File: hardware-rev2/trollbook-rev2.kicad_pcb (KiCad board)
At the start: 2 copper layers, 160 x 120 mm, 1 part, among them U1 MC68040FC33V

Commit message: added fpga
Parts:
- added U2: EPF10K50VRC240, mod:RQFP-240, F.Cu at (173.0, 101.5)
- moved U1 23.9 mm to (125.6, 101.1)

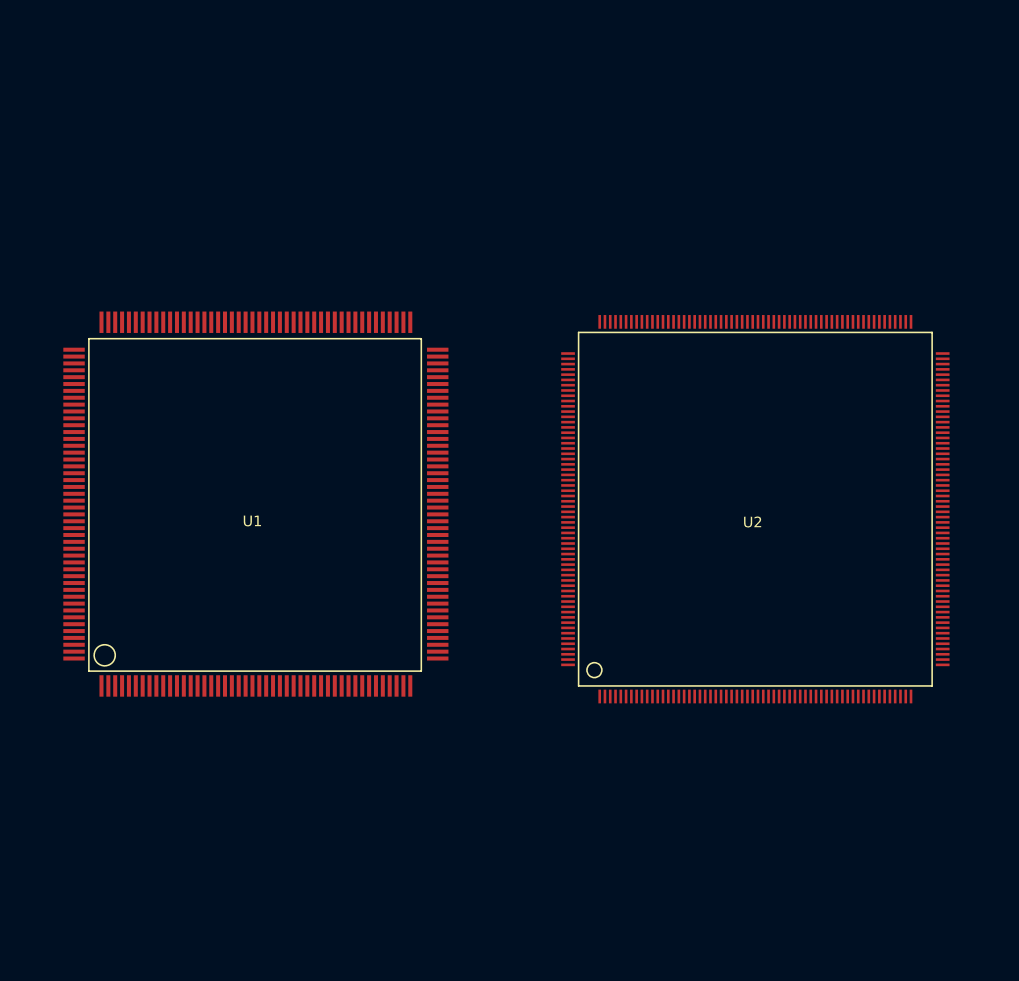
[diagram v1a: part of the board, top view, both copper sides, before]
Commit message: fixed clearance, added ram
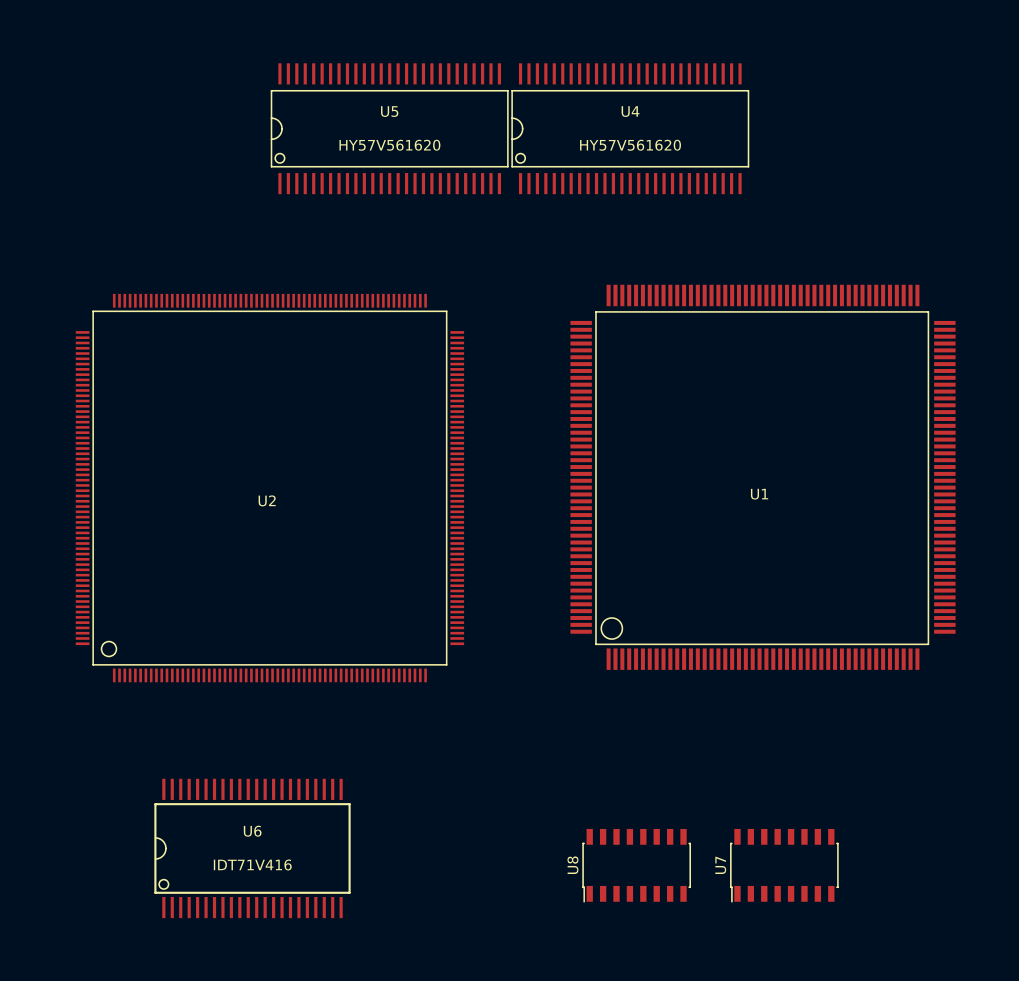
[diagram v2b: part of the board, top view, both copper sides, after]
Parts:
- added U4: HY57V561620, mod:TSOP54, F.Cu at (161.4, 65.2)
- added U5: HY57V561620, mod:TSOP54, F.Cu at (138.6, 65.2)
- added U6: IDT71V416, mod:TSOP44, F.Cu at (125.6, 133.4)
- added U7: TLC7524, Housings_SOIC:SOIC-16_3.9x9.9mm_Pitch1.27mm, F.Cu at (176.0, 135.0)
- added U8: TLC7524, Housings_SOIC:SOIC-16_3.9x9.9mm_Pitch1.27mm, F.Cu at (162.0, 135.0)
- moved U1 48.1 mm to (173.7, 98.6)
- moved U2 46.0 mm to (127.0, 99.5)
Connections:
- U1 pad 1: Net-(U1-Pad1) -> (no net)
- U1 pad 10: Net-(U1-Pad10) -> (no net)
- U1 pad 100: Net-(U1-Pad100) -> +3V3
- U1 pad 101: Net-(U1-Pad101) -> (no net)
- U1 pad 102: Net-(U1-Pad102) -> +3V3
- U1 pad 103: Net-(U1-Pad103) -> (no net)
- U1 pad 104: Net-(U1-Pad104) -> (no net)
- U1 pad 105: Net-(U1-Pad105) -> GND
- U1 pad 106: Net-(U1-Pad106) -> (no net)
- U1 pad 107: Net-(U1-Pad107) -> (no net)
- U1 pad 108: Net-(U1-Pad108) -> GND
- U1 pad 109: Net-(U1-Pad109) -> +3V3
- U1 pad 11: Net-(U1-Pad11) -> (no net)
- U1 pad 110: Net-(U1-Pad110) -> (no net)
- U1 pad 111: Net-(U1-Pad111) -> (no net)
- U1 pad 112: Net-(U1-Pad112) -> GND
- U1 pad 113: Net-(U1-Pad113) -> (no net)
- U1 pad 114: Net-(U1-Pad114) -> (no net)
- U1 pad 115: Net-(U1-Pad115) -> +3V3
- U1 pad 116: Net-(U1-Pad116) -> (no net)
- U1 pad 117: Net-(U1-Pad117) -> (no net)
- U1 pad 118: Net-(U1-Pad118) -> GND
- U1 pad 119: Net-(U1-Pad119) -> (no net)
- U1 pad 12: Net-(U1-Pad12) -> (no net)
- U1 pad 120: Net-(U1-Pad120) -> (no net)
- U1 pad 121: Net-(U1-Pad121) -> GND
- U1 pad 122: Net-(U1-Pad122) -> +3V3
- U1 pad 123: Net-(U1-Pad123) -> (no net)
- U1 pad 124: Net-(U1-Pad124) -> (no net)
- U1 pad 125: Net-(U1-Pad125) -> GND
- U1 pad 126: Net-(U1-Pad126) -> (no net)
- U1 pad 127: Net-(U1-Pad127) -> (no net)
- U1 pad 128: Net-(U1-Pad128) -> +3V3
- U1 pad 129: Net-(U1-Pad129) -> (no net)
- U1 pad 13: Net-(U1-Pad13) -> (no net)
- U1 pad 130: Net-(U1-Pad130) -> GND
- U1 pad 131: Net-(U1-Pad131) -> (no net)
- U1 pad 132: Net-(U1-Pad132) -> GND
- U1 pad 133: Net-(U1-Pad133) -> (no net)
- U1 pad 134: Net-(U1-Pad134) -> (no net)
- U1 pad 135: Net-(U1-Pad135) -> GND
- U1 pad 136: Net-(U1-Pad136) -> +3V3
- U1 pad 137: Net-(U1-Pad137) -> (no net)
- U1 pad 138: Net-(U1-Pad138) -> (no net)
- U1 pad 139: Net-(U1-Pad139) -> GND
- U1 pad 14: Net-(U1-Pad14) -> (no net)
- U1 pad 140: Net-(U1-Pad140) -> +3V3
- U1 pad 141: Net-(U1-Pad141) -> /A31
- U1 pad 142: Net-(U1-Pad142) -> /A30
- U1 pad 143: Net-(U1-Pad143) -> +3V3
- U1 pad 144: Net-(U1-Pad144) -> /A29
- U1 pad 145: Net-(U1-Pad145) -> /A28
- U1 pad 146: Net-(U1-Pad146) -> GND
- U1 pad 147: Net-(U1-Pad147) -> /A27
- U1 pad 148: Net-(U1-Pad148) -> /A26
- U1 pad 149: Net-(U1-Pad149) -> +3V3
- U1 pad 15: Net-(U1-Pad15) -> (no net)
- U1 pad 150: Net-(U1-Pad150) -> /A25
- U1 pad 151: Net-(U1-Pad151) -> /A24
- U1 pad 152: Net-(U1-Pad152) -> GND
- U1 pad 153: Net-(U1-Pad153) -> /A23
- U1 pad 154: Net-(U1-Pad154) -> /A22
- U1 pad 155: Net-(U1-Pad155) -> +3V3
- U1 pad 156: Net-(U1-Pad156) -> /A21
- U1 pad 157: Net-(U1-Pad157) -> /A20
- U1 pad 158: Net-(U1-Pad158) -> GND
- U1 pad 159: Net-(U1-Pad159) -> /A19
- U1 pad 16: Net-(U1-Pad16) -> +3V3
- U1 pad 160: Net-(U1-Pad160) -> /A18
- U1 pad 161: Net-(U1-Pad161) -> +3V3
- U1 pad 162: Net-(U1-Pad162) -> GND
- U1 pad 163: Net-(U1-Pad163) -> /A17
- U1 pad 164: Net-(U1-Pad164) -> /A16
- U1 pad 165: Net-(U1-Pad165) -> GND
- U1 pad 166: Net-(U1-Pad166) -> /A15
- U1 pad 167: Net-(U1-Pad167) -> /A14
- U1 pad 168: Net-(U1-Pad168) -> +3V3
- U1 pad 169: Net-(U1-Pad169) -> /A13
- U1 pad 17: Net-(U1-Pad17) -> GND
- U1 pad 170: Net-(U1-Pad170) -> /A12
- U1 pad 171: Net-(U1-Pad171) -> GND
- U1 pad 172: Net-(U1-Pad172) -> /A11
- U1 pad 173: Net-(U1-Pad173) -> /A10
- U1 pad 174: Net-(U1-Pad174) -> GND
- U1 pad 175: Net-(U1-Pad175) -> +3V3
- U1 pad 176: Net-(U1-Pad176) -> (no net)
- U1 pad 177: Net-(U1-Pad177) -> (no net)
- U1 pad 178: Net-(U1-Pad178) -> GND
- U1 pad 179: Net-(U1-Pad179) -> (no net)
- U1 pad 18: Net-(U1-Pad18) -> (no net)
- U1 pad 180: Net-(U1-Pad180) -> (no net)
- U1 pad 181: Net-(U1-Pad181) -> +3V3
- U1 pad 182: Net-(U1-Pad182) -> (no net)
- U1 pad 183: Net-(U1-Pad183) -> (no net)
- U1 pad 184: Net-(U1-Pad184) -> GND
- U1 pad 19: Net-(U1-Pad19) -> +3V3
- U1 pad 2: Net-(U1-Pad2) -> (no net)
- U1 pad 20: Net-(U1-Pad20) -> (no net)
- U1 pad 21: Net-(U1-Pad21) -> +3V3
- U1 pad 22: Net-(U1-Pad22) -> GND
- U1 pad 23: Net-(U1-Pad23) -> (no net)
- U1 pad 24: Net-(U1-Pad24) -> GND
- U1 pad 25: Net-(U1-Pad25) -> (no net)
- U1 pad 26: Net-(U1-Pad26) -> (no net)
- U1 pad 27: Net-(U1-Pad27) -> GND
- U1 pad 28: Net-(U1-Pad28) -> GND
- U1 pad 29: Net-(U1-Pad29) -> (no net)
- U1 pad 3: Net-(U1-Pad3) -> (no net)
- U1 pad 30: Net-(U1-Pad30) -> (no net)
- U1 pad 31: Net-(U1-Pad31) -> (no net)
- U1 pad 32: Net-(U1-Pad32) -> +3V3
- U1 pad 33: Net-(U1-Pad33) -> GND
- U1 pad 34: Net-(U1-Pad34) -> (no net)
- U1 pad 35: Net-(U1-Pad35) -> (no net)
- U1 pad 36: Net-(U1-Pad36) -> (no net)
- U1 pad 37: Net-(U1-Pad37) -> (no net)
- U1 pad 38: Net-(U1-Pad38) -> (no net)
- U1 pad 39: Net-(U1-Pad39) -> (no net)
- U1 pad 4: Net-(U1-Pad4) -> (no net)
- U1 pad 40: Net-(U1-Pad40) -> GND
- U1 pad 41: Net-(U1-Pad41) -> (no net)
- U1 pad 42: Net-(U1-Pad42) -> (no net)
- U1 pad 43: Net-(U1-Pad43) -> +3V3
- U1 pad 44: Net-(U1-Pad44) -> (no net)
- U1 pad 45: Net-(U1-Pad45) -> (no net)
- U1 pad 46: Net-(U1-Pad46) -> GND
- U1 pad 47: Net-(U1-Pad47) -> (no net)
- U1 pad 48: Net-(U1-Pad48) -> (no net)
- U1 pad 49: Net-(U1-Pad49) -> +3V3
- U1 pad 5: Net-(U1-Pad5) -> GND
- U1 pad 50: Net-(U1-Pad50) -> (no net)
- U1 pad 51: Net-(U1-Pad51) -> (no net)
- U1 pad 52: Net-(U1-Pad52) -> GND
- U1 pad 53: Net-(U1-Pad53) -> (no net)
- U1 pad 54: Net-(U1-Pad54) -> (no net)
- U1 pad 55: Net-(U1-Pad55) -> GND
- U1 pad 56: Net-(U1-Pad56) -> +3V3
- U1 pad 57: Net-(U1-Pad57) -> (no net)
- U1 pad 58: Net-(U1-Pad58) -> (no net)
- U1 pad 59: Net-(U1-Pad59) -> GND
- U1 pad 6: Net-(U1-Pad6) -> (no net)
- U1 pad 60: Net-(U1-Pad60) -> (no net)
- U1 pad 61: Net-(U1-Pad61) -> (no net)
- U1 pad 62: Net-(U1-Pad62) -> +3V3
- U1 pad 63: Net-(U1-Pad63) -> (no net)
- U1 pad 64: Net-(U1-Pad64) -> (no net)
- U1 pad 65: Net-(U1-Pad65) -> GND
- U1 pad 66: Net-(U1-Pad66) -> (no net)
- U1 pad 67: Net-(U1-Pad67) -> (no net)
- U1 pad 68: Net-(U1-Pad68) -> GND
- U1 pad 69: Net-(U1-Pad69) -> +3V3
- U1 pad 7: Net-(U1-Pad7) -> (no net)
- U1 pad 70: Net-(U1-Pad70) -> /A0
- U1 pad 71: Net-(U1-Pad71) -> /A1
- U1 pad 72: Net-(U1-Pad72) -> GND
- U1 pad 73: Net-(U1-Pad73) -> /A2
- U1 pad 74: Net-(U1-Pad74) -> /A3
- U1 pad 75: Net-(U1-Pad75) -> +3V3
- U1 pad 76: Net-(U1-Pad76) -> /A4
- U1 pad 77: Net-(U1-Pad77) -> /A5
- U1 pad 78: Net-(U1-Pad78) -> GND
- U1 pad 79: Net-(U1-Pad79) -> /A6
- U1 pad 8: Net-(U1-Pad8) -> GND
- U1 pad 80: Net-(U1-Pad80) -> /A7
- U1 pad 81: Net-(U1-Pad81) -> +3V3
- U1 pad 82: Net-(U1-Pad82) -> /A8
- U1 pad 83: Net-(U1-Pad83) -> /A9
- U1 pad 84: Net-(U1-Pad84) -> +3V3
- U1 pad 85: Net-(U1-Pad85) -> GND
- U1 pad 86: Net-(U1-Pad86) -> (no net)
- U1 pad 87: Net-(U1-Pad87) -> (no net)
- U1 pad 88: Net-(U1-Pad88) -> +3V3
- U1 pad 89: Net-(U1-Pad89) -> (no net)
- U1 pad 9: Net-(U1-Pad9) -> +3V3
- U1 pad 90: Net-(U1-Pad90) -> (no net)
- U1 pad 91: Net-(U1-Pad91) -> GND
- U1 pad 92: Net-(U1-Pad92) -> (no net)
- U1 pad 93: Net-(U1-Pad93) -> (no net)
- U1 pad 94: Net-(U1-Pad94) -> +3V3
- U1 pad 95: Net-(U1-Pad95) -> GND
- U1 pad 96: Net-(U1-Pad96) -> (no net)
- U1 pad 97: Net-(U1-Pad97) -> (no net)
- U1 pad 98: Net-(U1-Pad98) -> GND
- U1 pad 99: Net-(U1-Pad99) -> (no net)
- U2 pad 1: Net-(U2-Pad1) -> (no net)
- U2 pad 10: Net-(U2-Pad10) -> GND
- U2 pad 100: Net-(U2-Pad100) -> /A13
- U2 pad 101: Net-(U2-Pad101) -> /A14
- U2 pad 102: Net-(U2-Pad102) -> /A15
- U2 pad 103: Net-(U2-Pad103) -> /A16
- U2 pad 104: Net-(U2-Pad104) -> GND
- U2 pad 105: Net-(U2-Pad105) -> /A17
- U2 pad 106: Net-(U2-Pad106) -> /A18
- U2 pad 107: Net-(U2-Pad107) -> /A19
- U2 pad 108: Net-(U2-Pad108) -> /A20
- U2 pad 109: Net-(U2-Pad109) -> /A21
- U2 pad 11: Net-(U2-Pad11) -> (no net)
- U2 pad 110: Net-(U2-Pad110) -> /A22
- U2 pad 111: Net-(U2-Pad111) -> /A23
- U2 pad 112: Net-(U2-Pad112) -> +3V3
- U2 pad 113: Net-(U2-Pad113) -> /A24
- U2 pad 114: Net-(U2-Pad114) -> /A25
- U2 pad 115: Net-(U2-Pad115) -> /A26
- U2 pad 116: Net-(U2-Pad116) -> /A27
- U2 pad 117: Net-(U2-Pad117) -> /A28
- U2 pad 118: Net-(U2-Pad118) -> /A29
- U2 pad 119: Net-(U2-Pad119) -> /A30
- U2 pad 12: Net-(U2-Pad12) -> (no net)
- U2 pad 120: Net-(U2-Pad120) -> /A31
- U2 pad 121: Net-(U2-Pad121) -> (no net)
- U2 pad 122: Net-(U2-Pad122) -> +3V3
- U2 pad 123: Net-(U2-Pad123) -> (no net)
- U2 pad 124: Net-(U2-Pad124) -> (no net)
- U2 pad 125: Net-(U2-Pad125) -> GND
- U2 pad 126: Net-(U2-Pad126) -> (no net)
- U2 pad 127: Net-(U2-Pad127) -> (no net)
- U2 pad 128: Net-(U2-Pad128) -> (no net)
- U2 pad 129: Net-(U2-Pad129) -> (no net)
- U2 pad 13: Net-(U2-Pad13) -> (no net)
- U2 pad 130: Net-(U2-Pad130) -> +3V3
- U2 pad 131: Net-(U2-Pad131) -> (no net)
- U2 pad 132: Net-(U2-Pad132) -> (no net)
- U2 pad 133: Net-(U2-Pad133) -> (no net)
- U2 pad 134: Net-(U2-Pad134) -> (no net)
- U2 pad 135: Net-(U2-Pad135) -> GND
- U2 pad 136: Net-(U2-Pad136) -> (no net)
- U2 pad 137: Net-(U2-Pad137) -> (no net)
- U2 pad 138: Net-(U2-Pad138) -> (no net)
- U2 pad 139: Net-(U2-Pad139) -> (no net)
- U2 pad 14: Net-(U2-Pad14) -> (no net)
- U2 pad 140: Net-(U2-Pad140) -> +3V3
- U2 pad 141: Net-(U2-Pad141) -> (no net)
- U2 pad 142: Net-(U2-Pad142) -> (no net)
- U2 pad 143: Net-(U2-Pad143) -> (no net)
- U2 pad 144: Net-(U2-Pad144) -> (no net)
- U2 pad 145: Net-(U2-Pad145) -> GND
- U2 pad 146: Net-(U2-Pad146) -> (no net)
- U2 pad 147: Net-(U2-Pad147) -> (no net)
- U2 pad 148: Net-(U2-Pad148) -> (no net)
- U2 pad 149: Net-(U2-Pad149) -> (no net)
- U2 pad 15: Net-(U2-Pad15) -> (no net)
- U2 pad 150: Net-(U2-Pad150) -> +3V3
- U2 pad 151: Net-(U2-Pad151) -> (no net)
- U2 pad 152: Net-(U2-Pad152) -> (no net)
- U2 pad 153: Net-(U2-Pad153) -> (no net)
- U2 pad 154: Net-(U2-Pad154) -> (no net)
- U2 pad 155: Net-(U2-Pad155) -> GND
- U2 pad 156: Net-(U2-Pad156) -> (no net)
- U2 pad 157: Net-(U2-Pad157) -> (no net)
- U2 pad 158: Net-(U2-Pad158) -> (no net)
- U2 pad 159: Net-(U2-Pad159) -> (no net)
- U2 pad 16: Net-(U2-Pad16) -> +3V3
- U2 pad 160: Net-(U2-Pad160) -> +3V3
- U2 pad 161: Net-(U2-Pad161) -> (no net)
- U2 pad 162: Net-(U2-Pad162) -> (no net)
- U2 pad 163: Net-(U2-Pad163) -> (no net)
- U2 pad 164: Net-(U2-Pad164) -> (no net)
- U2 pad 165: Net-(U2-Pad165) -> GND
- U2 pad 166: Net-(U2-Pad166) -> (no net)
- U2 pad 167: Net-(U2-Pad167) -> (no net)
- U2 pad 168: Net-(U2-Pad168) -> (no net)
- U2 pad 169: Net-(U2-Pad169) -> (no net)
- U2 pad 17: Net-(U2-Pad17) -> (no net)
- U2 pad 170: Net-(U2-Pad170) -> +3V3
- U2 pad 171: Net-(U2-Pad171) -> (no net)
- U2 pad 172: Net-(U2-Pad172) -> (no net)
- U2 pad 173: Net-(U2-Pad173) -> (no net)
- U2 pad 174: Net-(U2-Pad174) -> (no net)
- U2 pad 175: Net-(U2-Pad175) -> (no net)
- U2 pad 176: Net-(U2-Pad176) -> GND
- U2 pad 177: Net-(U2-Pad177) -> (no net)
- U2 pad 178: Net-(U2-Pad178) -> (no net)
- U2 pad 179: Net-(U2-Pad179) -> (no net)
- U2 pad 18: Net-(U2-Pad18) -> (no net)
- U2 pad 180: Net-(U2-Pad180) -> (no net)
- U2 pad 181: Net-(U2-Pad181) -> (no net)
- U2 pad 182: Net-(U2-Pad182) -> (no net)
- U2 pad 183: Net-(U2-Pad183) -> (no net)
- U2 pad 184: Net-(U2-Pad184) -> (no net)
- U2 pad 185: Net-(U2-Pad185) -> (no net)
- U2 pad 186: Net-(U2-Pad186) -> (no net)
- U2 pad 187: Net-(U2-Pad187) -> (no net)
- U2 pad 188: Net-(U2-Pad188) -> (no net)
- U2 pad 189: Net-(U2-Pad189) -> +3V3
- U2 pad 19: Net-(U2-Pad19) -> (no net)
- U2 pad 190: Net-(U2-Pad190) -> (no net)
- U2 pad 191: Net-(U2-Pad191) -> (no net)
- U2 pad 192: Net-(U2-Pad192) -> (no net)
- U2 pad 193: Net-(U2-Pad193) -> (no net)
- U2 pad 194: Net-(U2-Pad194) -> (no net)
- U2 pad 195: Net-(U2-Pad195) -> (no net)
- U2 pad 196: Net-(U2-Pad196) -> (no net)
- U2 pad 197: Net-(U2-Pad197) -> GND
- U2 pad 198: Net-(U2-Pad198) -> (no net)
- U2 pad 199: Net-(U2-Pad199) -> (no net)
- U2 pad 2: Net-(U2-Pad2) -> (no net)
- U2 pad 20: Net-(U2-Pad20) -> (no net)
- U2 pad 200: Net-(U2-Pad200) -> (no net)
- U2 pad 201: Net-(U2-Pad201) -> (no net)
- U2 pad 202: Net-(U2-Pad202) -> (no net)
- U2 pad 203: Net-(U2-Pad203) -> (no net)
- U2 pad 204: Net-(U2-Pad204) -> (no net)
- U2 pad 205: Net-(U2-Pad205) -> +3V3
- U2 pad 206: Net-(U2-Pad206) -> (no net)
- U2 pad 207: Net-(U2-Pad207) -> (no net)
- U2 pad 208: Net-(U2-Pad208) -> (no net)
- U2 pad 209: Net-(U2-Pad209) -> (no net)
- U2 pad 21: Net-(U2-Pad21) -> (no net)
- U2 pad 210: Net-(U2-Pad210) -> (no net)
- U2 pad 211: Net-(U2-Pad211) -> (no net)
- U2 pad 212: Net-(U2-Pad212) -> (no net)
- U2 pad 213: Net-(U2-Pad213) -> (no net)
- U2 pad 214: Net-(U2-Pad214) -> (no net)
- U2 pad 215: Net-(U2-Pad215) -> (no net)
- U2 pad 216: Net-(U2-Pad216) -> GND
- U2 pad 217: Net-(U2-Pad217) -> (no net)
- U2 pad 218: Net-(U2-Pad218) -> (no net)
- U2 pad 219: Net-(U2-Pad219) -> (no net)
- U2 pad 22: Net-(U2-Pad22) -> GND
- U2 pad 220: Net-(U2-Pad220) -> (no net)
- U2 pad 221: Net-(U2-Pad221) -> (no net)
- U2 pad 222: Net-(U2-Pad222) -> (no net)
- U2 pad 223: Net-(U2-Pad223) -> (no net)
- U2 pad 224: Net-(U2-Pad224) -> +3V3
- U2 pad 225: Net-(U2-Pad225) -> (no net)
- U2 pad 226: Net-(U2-Pad226) -> (no net)
- U2 pad 227: Net-(U2-Pad227) -> (no net)
- U2 pad 228: Net-(U2-Pad228) -> (no net)
- U2 pad 229: Net-(U2-Pad229) -> (no net)
- U2 pad 23: Net-(U2-Pad23) -> (no net)
- U2 pad 230: Net-(U2-Pad230) -> (no net)
- U2 pad 231: Net-(U2-Pad231) -> (no net)
- U2 pad 232: Net-(U2-Pad232) -> GND
- U2 pad 233: Net-(U2-Pad233) -> (no net)
- U2 pad 234: Net-(U2-Pad234) -> (no net)
- U2 pad 235: Net-(U2-Pad235) -> (no net)
- U2 pad 236: Net-(U2-Pad236) -> (no net)
- U2 pad 237: Net-(U2-Pad237) -> (no net)
- U2 pad 238: Net-(U2-Pad238) -> (no net)
- U2 pad 239: Net-(U2-Pad239) -> (no net)
- U2 pad 24: Net-(U2-Pad24) -> (no net)
- U2 pad 240: Net-(U2-Pad240) -> (no net)
- U2 pad 25: Net-(U2-Pad25) -> (no net)
- U2 pad 26: Net-(U2-Pad26) -> (no net)
- U2 pad 27: Net-(U2-Pad27) -> +3V3
- U2 pad 28: Net-(U2-Pad28) -> (no net)
- U2 pad 29: Net-(U2-Pad29) -> (no net)
- U2 pad 3: Net-(U2-Pad3) -> (no net)
- U2 pad 30: Net-(U2-Pad30) -> (no net)
- U2 pad 31: Net-(U2-Pad31) -> (no net)
- U2 pad 32: Net-(U2-Pad32) -> GND
- U2 pad 33: Net-(U2-Pad33) -> (no net)
- U2 pad 34: Net-(U2-Pad34) -> (no net)
- U2 pad 35: Net-(U2-Pad35) -> (no net)
- U2 pad 36: Net-(U2-Pad36) -> (no net)
- U2 pad 37: Net-(U2-Pad37) -> +3V3
- U2 pad 38: Net-(U2-Pad38) -> (no net)
- U2 pad 39: Net-(U2-Pad39) -> (no net)
- U2 pad 4: Net-(U2-Pad4) -> (no net)
- U2 pad 40: Net-(U2-Pad40) -> (no net)
- U2 pad 41: Net-(U2-Pad41) -> (no net)
- U2 pad 42: Net-(U2-Pad42) -> GND
- U2 pad 43: Net-(U2-Pad43) -> (no net)
- U2 pad 44: Net-(U2-Pad44) -> (no net)
- U2 pad 45: Net-(U2-Pad45) -> (no net)
- U2 pad 46: Net-(U2-Pad46) -> (no net)
- U2 pad 47: Net-(U2-Pad47) -> +3V3
- U2 pad 48: Net-(U2-Pad48) -> (no net)
- U2 pad 49: Net-(U2-Pad49) -> (no net)
- U2 pad 5: Net-(U2-Pad5) -> +3V3
- U2 pad 50: Net-(U2-Pad50) -> (no net)
- U2 pad 51: Net-(U2-Pad51) -> (no net)
- U2 pad 52: Net-(U2-Pad52) -> GND
- U2 pad 53: Net-(U2-Pad53) -> (no net)
- U2 pad 54: Net-(U2-Pad54) -> (no net)
- U2 pad 55: Net-(U2-Pad55) -> (no net)
- U2 pad 56: Net-(U2-Pad56) -> (no net)
- U2 pad 57: Net-(U2-Pad57) -> +3V3
- U2 pad 58: Net-(U2-Pad58) -> (no net)
- U2 pad 59: Net-(U2-Pad59) -> (no net)
- U2 pad 6: Net-(U2-Pad6) -> (no net)
- U2 pad 60: Net-(U2-Pad60) -> (no net)
- U2 pad 61: Net-(U2-Pad61) -> (no net)
- U2 pad 62: Net-(U2-Pad62) -> (no net)
- U2 pad 63: Net-(U2-Pad63) -> (no net)
- U2 pad 64: Net-(U2-Pad64) -> (no net)
- U2 pad 65: Net-(U2-Pad65) -> (no net)
- U2 pad 66: Net-(U2-Pad66) -> (no net)
- U2 pad 67: Net-(U2-Pad67) -> (no net)
- U2 pad 68: Net-(U2-Pad68) -> (no net)
- U2 pad 69: Net-(U2-Pad69) -> GND
- U2 pad 7: Net-(U2-Pad7) -> (no net)
- U2 pad 70: Net-(U2-Pad70) -> (no net)
- U2 pad 71: Net-(U2-Pad71) -> (no net)
- U2 pad 72: Net-(U2-Pad72) -> (no net)
- U2 pad 73: Net-(U2-Pad73) -> (no net)
- U2 pad 74: Net-(U2-Pad74) -> (no net)
- U2 pad 75: Net-(U2-Pad75) -> (no net)
- U2 pad 76: Net-(U2-Pad76) -> (no net)
- U2 pad 77: Net-(U2-Pad77) -> +3V3
- U2 pad 78: Net-(U2-Pad78) -> (no net)
- U2 pad 79: Net-(U2-Pad79) -> (no net)
- U2 pad 8: Net-(U2-Pad8) -> (no net)
- U2 pad 80: Net-(U2-Pad80) -> /A0
- U2 pad 81: Net-(U2-Pad81) -> /A1
- U2 pad 82: Net-(U2-Pad82) -> /A2
- U2 pad 83: Net-(U2-Pad83) -> /A3
- U2 pad 84: Net-(U2-Pad84) -> /A4
- U2 pad 85: Net-(U2-Pad85) -> GND
- U2 pad 86: Net-(U2-Pad86) -> /A5
- U2 pad 87: Net-(U2-Pad87) -> /A6
- U2 pad 88: Net-(U2-Pad88) -> /A7
- U2 pad 89: Net-(U2-Pad89) -> +3V3
- U2 pad 9: Net-(U2-Pad9) -> (no net)
- U2 pad 90: Net-(U2-Pad90) -> (no net)
- U2 pad 91: Net-(U2-Pad91) -> (no net)
- U2 pad 92: Net-(U2-Pad92) -> (no net)
- U2 pad 93: Net-(U2-Pad93) -> GND
- U2 pad 94: Net-(U2-Pad94) -> /A8
- U2 pad 95: Net-(U2-Pad95) -> /A9
- U2 pad 96: Net-(U2-Pad96) -> +3V3
- U2 pad 97: Net-(U2-Pad97) -> /A10
- U2 pad 98: Net-(U2-Pad98) -> /A11
- U2 pad 99: Net-(U2-Pad99) -> /A12
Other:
- rule pad_to_mask_clearance: 0.2 -> 0.0508

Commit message: track width
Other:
- net class Default: clearance 0.2 -> 0.2032; trace_width 0.25 -> 0.2032
- rule trace_clearance: 0.2 -> 0.2032

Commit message: arne
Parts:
- moved U6 102.8 mm to (227.5, 119.7)
- moved U7 63.9 mm to (239.8, 138.6)
- moved U8 63.9 mm to (225.8, 138.6)
- moved U5 52.2 mm to (185.9, 87.2)
- moved U1 25.2 mm to (171.5, 123.6)
- moved U4 22.0 mm to (162.4, 87.2)
- moved U2 21.8 mm to (124.9, 77.8)
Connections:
- U1 pad 101: (no net) -> /D22
- U1 pad 103: (no net) -> /D21
- U1 pad 104: (no net) -> /D20
- U1 pad 106: (no net) -> /D19
- U1 pad 107: (no net) -> /D18
- U1 pad 110: (no net) -> /D17
- U1 pad 111: (no net) -> /D16
- U1 pad 113: (no net) -> /D15
- U1 pad 114: (no net) -> /D14
- U1 pad 116: (no net) -> /D13
- U1 pad 117: (no net) -> /D12
- U1 pad 119: (no net) -> /D11
- U1 pad 120: (no net) -> /D10
- U1 pad 123: (no net) -> /D9
- U1 pad 124: (no net) -> /D8
- U1 pad 126: (no net) -> /D7
- U1 pad 127: (no net) -> /D6
- U1 pad 129: (no net) -> /D5
- U1 pad 131: (no net) -> /D4
- U1 pad 133: (no net) -> /D3
- U1 pad 134: (no net) -> /D2
- U1 pad 137: (no net) -> /D1
- U1 pad 138: (no net) -> /D0
- U1 pad 86: (no net) -> /D31
- U1 pad 87: (no net) -> /D30
- U1 pad 89: (no net) -> /D29
- U1 pad 90: (no net) -> /D28
- U1 pad 92: (no net) -> /D27
- U1 pad 93: (no net) -> /D26
- U1 pad 96: (no net) -> /D25
- U1 pad 97: (no net) -> /D24
- U1 pad 99: (no net) -> /D23
- U2 pad 39: (no net) -> /D0
- U2 pad 40: (no net) -> /D1
- U2 pad 41: (no net) -> /D2
- U2 pad 43: (no net) -> /D3
- U2 pad 44: (no net) -> /D4
- U2 pad 45: (no net) -> /D5
- U2 pad 46: (no net) -> /D6
- U2 pad 48: (no net) -> /D7
- U2 pad 49: (no net) -> /D8
- U2 pad 50: (no net) -> /D9
- U2 pad 51: (no net) -> /D10
- U2 pad 53: (no net) -> /D11
- U2 pad 54: (no net) -> /D12
- U2 pad 55: (no net) -> /D13
- U2 pad 56: (no net) -> /D14
- U2 pad 61: (no net) -> /D15
- U2 pad 62: (no net) -> /D16
- U2 pad 63: (no net) -> /D17
- U2 pad 64: (no net) -> /D18
- U2 pad 65: (no net) -> /D19
- U2 pad 66: (no net) -> /D20
- U2 pad 67: (no net) -> /D21
- U2 pad 68: (no net) -> /D22
- U2 pad 70: (no net) -> /D23
- U2 pad 71: (no net) -> /D24
- U2 pad 72: (no net) -> /D25
- U2 pad 73: (no net) -> /D26
- U2 pad 74: (no net) -> /D27
- U2 pad 75: (no net) -> /D28
- U2 pad 76: (no net) -> /D29
- U2 pad 78: (no net) -> /D30
- U2 pad 79: (no net) -> /D31
- U4 pad 10: (no net) -> /D5
- U4 pad 11: (no net) -> /D6
- U4 pad 13: (no net) -> /D7
- U4 pad 2: (no net) -> /D0
- U4 pad 4: (no net) -> /D1
- U4 pad 42: (no net) -> /D8
- U4 pad 44: (no net) -> /D9
- U4 pad 45: (no net) -> /D10
- U4 pad 47: (no net) -> /D11
- U4 pad 48: (no net) -> /D12
- U4 pad 5: (no net) -> /D2
- U4 pad 50: (no net) -> /D13
- U4 pad 51: (no net) -> /D14
- U4 pad 53: (no net) -> /D15
- U4 pad 7: (no net) -> /D3
- U4 pad 8: (no net) -> /D4
- U5 pad 10: (no net) -> /D21
- U5 pad 11: (no net) -> /D22
- U5 pad 13: (no net) -> /D23
- U5 pad 2: (no net) -> /D16
- U5 pad 4: (no net) -> /D17
- U5 pad 42: (no net) -> /D24
- U5 pad 44: (no net) -> /D25
- U5 pad 45: (no net) -> /D26
- U5 pad 47: (no net) -> /D27
- U5 pad 48: (no net) -> /D28
- U5 pad 5: (no net) -> /D18
- U5 pad 50: (no net) -> /D29
- U5 pad 51: (no net) -> /D30
- U5 pad 53: (no net) -> /D31
- U5 pad 7: (no net) -> /D19
- U5 pad 8: (no net) -> /D20
